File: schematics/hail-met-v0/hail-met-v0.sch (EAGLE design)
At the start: 8 parts, among them U1 ATMEGA328P, X1 S4B-ZR, Y1 16MHZ

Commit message: updated schematic, added datasheets
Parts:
- removed X1: S4B-ZR, con-jst:S4B-ZR
- added C3: 4700uF, rcl:CPOL-USE5-13
- added C4: 10uF, adafruit:C-USC0805K
- added C5: 10uF, rcl:C-USC0805K
- added CHRG/LBO: ORANGE, adafruit:LEDCHIP-LED0805
- added DONE: GREEN, adafruit:LEDCHIP-LED0805
- added IC1: MCP73871, adafruit:MCP73871
- added JP_BATT, JP_SOLAR: (no value), adafruit:JST_2PIN-SMT-RA
- added PWR: RED, adafruit:LEDCHIP-LED0805
- added R10: 150K, rcl:R-US_M0805
- added R11: 100K, rcl:R-US_M0805
- added R12: 2K, adafruit:R-US_FLIPFLOP
- added R3, R4: (no value), SparkFun-Resistors:1KOHM1/10W1%(0603)
- added R5, R6, R7: 1K, SparkFun-Resistors:1KOHM1/10W1%(0603)
- added R8: 1K, rcl:R-US_M0805
- added R9: 10K, adafruit:R-US_FLIPFLOP
- added U$2: 10118193, MicroUSB:10118193
- added U2: TLC5917ID, Texas Instruments_By_element14_Batch_1:TLC5917ID
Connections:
- new net LED_OE: U1.PB1(OC1A), U2.~OE(ED2)
- new net N$10: U2.~OUT5
- new net N$11: U2.~OUT6
- new net N$12: U2.~OUT7
- new net N$13: R10.2, R8.2, R9.2
- new net N$14: U2.LE(ED1)
- new net N$15: U2.SDI
- new net N$16: U2.CLK
- new net N$17: IC1.VPCC, R3.2, R4.1
- new net N$18: IC1.PROG3, R11.2
- new net N$19: IC1./PG, PWR.C
- new net N$20: DONE.C, IC1.STAT2
- new net N$21: CHRG/LBO.C, IC1.STAT1/LBO
- new net N$22: CHRG/LBO.A, R7.1
- new net N$23: DONE.A, R6.1
- new net N$24: PWR.A, R5.1
- new net N$26: C5.1, IC1.VBAT1, IC1.VBAT2, IC1.VBAT3, JP_BATT.1
- new net N$3: IC1.THERM, R8.1
- new net N$5: U2.~OUT0
- new net N$6: U2.~OUT1
- new net N$7: U2.~OUT2
- new net N$8: U2.~OUT3
- new net N$9: U2.~OUT4
- new net PROG1: IC1.PROG1, R12.2
- new net VCC: C3.+, C4.1, IC1./TE, IC1.CE, IC1.IN1, IC1.IN2, IC1.PROG2, IC1.SEL, JP_SOLAR.1, R4.2, R5.2, R6.2, R7.2, U$2.VBUS
- net 3.3V: now also U2.VDD
- net GND: now also C3.-, C4.2, C5.2, IC1.GND1, IC1.GND2, JP_BATT.2, JP_SOLAR.2, R10.1, R11.1, R12.1, R3.1, R9.1, U$2.GND, U2.GND
- net VIN: now also IC1.OUT1, IC1.OUT2
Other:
- note added: "1.0K = 1000mA"
- note added: "10K NTC Thermistor:"
- note added: "2.0K = 500mA"
- note added: "Charge Rate = 1000V/PROG1"
- note added: "JST jack to batteries"
- note added: "LED Driver"
- note added: "NEED TO SET THIS TO VREG. For 6V solar panel, use 1KOhm / 1KOhm"
- note added: "No Thermistor:"
- note added: "Power input (USB, Solar)"
- note added: "RT1 = 0, RT2 = 10K"
- note added: "RT1 = TBD, RT2 = TBD"
- note added: "Voltage regulator for microcontroller"
- note removed: "JST jack from batteries"
- moved on the sheet: C1, C2, R1, R2, U$1

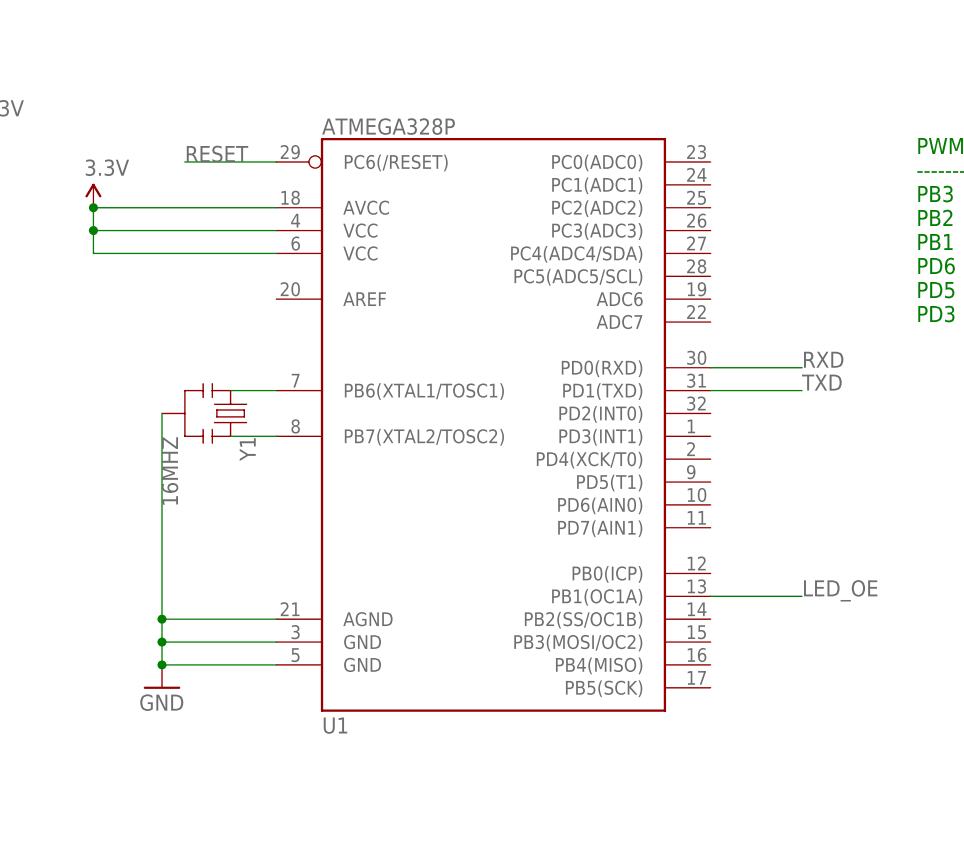
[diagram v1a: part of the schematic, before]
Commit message: cleaned up EAGLE temp files
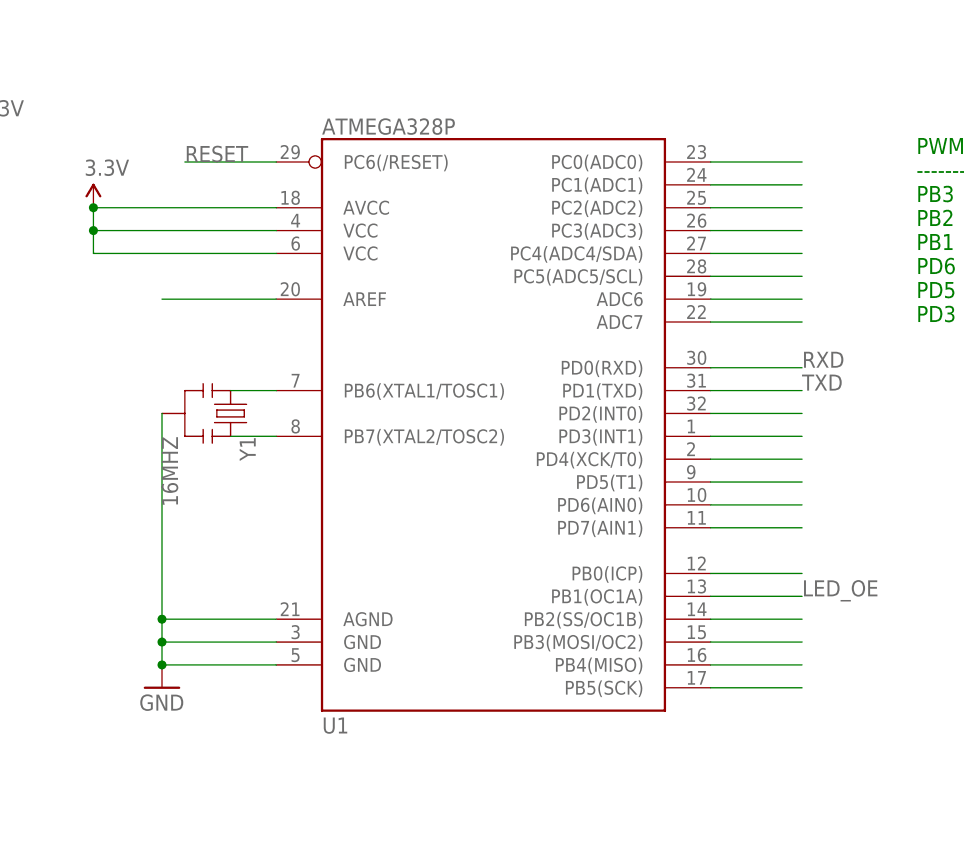
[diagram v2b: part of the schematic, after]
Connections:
- new net N$25: U1.AREF
- new net N$27: U1.PC0(ADC0)
- new net N$28: U1.PC1(ADC1)
- new net N$29: U1.PC2(ADC2)
- new net N$30: U1.PC3(ADC3)
- new net N$31: U1.PC4(ADC4/SDA)
- new net N$32: U1.PC5(ADC5/SCL)
- new net N$33: U1.ADC6
- new net N$34: U1.ADC7
- new net N$35: U1.PD2(INT0)
- new net N$36: U1.PD3(INT1)
- new net N$37: U1.PD4(XCK/T0)
- new net N$38: U1.PD5(T1)
- new net N$39: U1.PD6(AIN0)
- new net N$40: U1.PD7(AIN1)
- new net N$41: U1.PB0(ICP)
- new net N$42: U1.PB2(SS/OC1B)
- new net N$43: U1.PB3(MOSI/OC2)
- new net N$44: U1.PB4(MISO)
- new net N$45: U1.PB5(SCK)
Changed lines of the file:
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@@
+</segment>
+</net>
+<net name="N$25" class="0">
+<segment>
+<pinref part="U1" gate="G$1" pin="AREF"/>
+<wire x1="83.82" y1="71.12" x2="71.12" y2="71.12" width="0.1524" layer="91"/>
+</segment>
+</net>
+<net name="N$27" class="0">
+<segment>
+<pinref part="U1" gate="G$1" pin="PC0(ADC0)"/>
+<wire x1="132.08" y1="86.36" x2="142.24" y2="86.36" width="0.1524" layer="91"/>
+</segment>
+</net>
+<net name="N$28" class="0">
+<segment>
+<pinref part="U1" gate="G$1" pin="PC1(ADC1)"/>
+<wire x1="132.08" y1="83.82" x2="142.24" y2="83.82" width="0.1524" layer="91"/>
+</segment>
+</net>
+<net name="N$29" class="0">
+<segment>
+<pinref part="U1" gate="G$1" pin="PC2(ADC2)"/>
+<wire x1="132.08" y1="81.28" x2="142.24" y2="81.28" width="0.1524" layer="91"/>
+</segment>
+</net>
+<net name="N$30" class="0">
+<segment>
+<pinref part="U1" gate="G$1" pin="PC3(ADC3)"/>
+<wire x1="132.08" y1="78.74" x2="142.24" y2="78.74" width="0.1524" layer="91"/>
+</segment>
+</net>
+<net name="N$31" class="0">
+<segment>
+<pinref part="U1" gate="G$1" pin="PC4(ADC4/SDA)"/>
+<wire x1="132.08" y1="76.2" x2="142.24" y2="76.2" width="0.1524" layer="91"/>
+</segment>
+</net>
+<net name="N$32" class="0">
+<segment>
+<pinref part="U1" gate="G$1" pin="PC5(ADC5/SCL)"/>
+<wire x1="132.08" y1="73.66" x2="142.24" y2="73.66" width="0.1524" layer="91"/>
+</segment>
+</net>
+<net name="N$33" class="0">
+<segment>
+<pinref part="U1" gate="G$1" pin="ADC6"/>
+<wire x1="132.08" y1="71.12" x2="142.24" y2="71.12" width="0.1524" layer="91"/>
+</segment>
+</net>
+<net name="N$34" class="0">
+<segment>
+<pinref part="U1" gate="G$1" pin="ADC7"/>
+<wire x1="132.08" y1="68.58" x2="142.24" y2="68.58" width="0.1524" layer="91"/>
+</segment>
+</net>
+<net name="N$35" class="0">
+<segment>
+<pinref part="U1" gate="G$1" pin="PD2(INT0)"/>
+<wire x1="132.08" y1="58.42" x2="142.24" y2="58.42" width="0.1524" layer="91"/>
+</segment>
+</net>
+<net name="N$36" class="0">
+<segment>
+<pinref part="U1" gate="G$1" pin="PD3(INT1)"/>
+<wire x1="132.08" y1="55.88" x2="142.24" y2="55.88" width="0.1524" layer="91"/>
+</segment>
+</net>
+<net name="N$37" class="0">
+<segment>
+<pinref part="U1" gate="G$1" pin="PD4(XCK/T0)"/>
+<wire x1="132.08" y1="53.34" x2="142.24" y2="53.34" width="0.1524" layer="91"/>
+</segment>
+</net>
+<net name="N$38" class="0">
+<segment>
+<pinref part="U1" gate="G$1" pin="PD5(T1)"/>
+<wire x1="132.08" y1="50.8" x2="142.24" y2="50.8" width="0.1524" layer="91"/>
+</segment>
+</net>
+<net name="N$39" class="0">
+<segment>
+<pinref part="U1" gate="G$1" pin="PD6(AIN0)"/>
+<wire x1="132.08" y1="48.26" x2="142.24" y2="48.26" width="0.1524" layer="91"/>
+</segment>
+</net>
+<net name="N$40" class="0">
+<segment>
+<pinref part="U1" gate="G$1" pin="PD7(AIN1)"/>
+<wire x1="132.08" y1="45.72" x2="142.24" y2="45.72" width="0.1524" layer="91"/>
+</segment>
+</net>
+<net name="N$41" class="0">
+<segment>
+<pinref part="U1" gate="G$1" pin="PB0(ICP)"/>
+<wire x1="132.08" y1="40.64" x2="142.24" y2="40.64" width="0.1524" layer="91"/>
+</segment>
+</net>
+<net name="N$42" class="0">
+<segment>
+<pinref part="U1" gate="G$1" pin="PB2(SS/OC1B)"/>
+<wire x1="132.08" y1="35.56" x2="142.24" y2="35.56" width="0.1524" layer="91"/>
+</segment>
+</net>
+<net name="N$43" class="0">
+<segment>
+<pinref part="U1" gate="G$1" pin="PB3(MOSI/OC2)"/>
+<wire x1="132.08" y1="33.02" x2="142.24" y2="33.02" width="0.1524" layer="91"/>
+</segment>
+</net>
+<net name="N$44" class="0">
+<segment>
+<pinref part="U1" gate="G$1" pin="PB4(MISO)"/>
+<wire x1="132.08" y1="30.48" x2="142.24" y2="30.48" width="0.1524" layer="91"/>
+</segment>
+</net>
+<net name="N$45" class="0">
+<segment>
+<pinref part="U1" gate="G$1" pin="PB5(SCK)"/>
+<wire x1="132.08" y1="27.94" x2="142.24" y2="27.94" width="0.1524" layer="91"/>
 </segment>
 </net>

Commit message: updated schematic
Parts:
- added C6: 0.1uF, SparkFun-Capacitors:0.1UF-25V-5%(0603)
- added FTDI: (no value), SparkFun:M06SIP
- added JP10, JP11, JP9, LED0, LED1, LED2, LED3, LED4, LED5, LED6, LED7: M02PTH, SparkFun-Connectors:M02PTH
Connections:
- net N$26 renamed VBATT
- net N$32 renamed PC5
- net VCC renamed VCHG
- removed net N$15: U2.SDI
- removed net N$16: U2.CLK
- removed net N$43: U1.PB3(MOSI/OC2)
- removed net N$45: U1.PB5(SCK)
- new net CTS: C6.2, FTDI.2
- new net DTR: FTDI.6
- new net LED_CLK: U1.PB5(SCK), U2.CLK
- new net LED_SDI: U1.PB3(MOSI/OC2), U2.SDI
- net 3.3V: now also FTDI.3, LED0.1, LED1.1, LED2.1, LED3.1, LED4.1, LED5.1, LED6.1, LED7.1
- net GND: now also FTDI.1
- net N$10: now also LED5.2
- net N$11: now also LED6.2
- net N$12: now also LED7.2
- net N$5: now also LED0.2
- net N$6: now also LED1.2
- net N$7: now also LED2.2
- net N$8: now also LED3.2
- net N$9: now also LED4.2
- net RESET: now also C6.1
- net RXD: now also FTDI.4
- net TXD: now also FTDI.5
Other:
- note added: "Bluetooth"
- note added: "DONE"
- note added: "Design: Validate:"
- note added: "Done, need VCC resistor check"
- moved on the sheet: C1, C2, R1, R2, U$1, U2

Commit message: worked on schematic
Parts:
- removed JP10, JP9, LED0, LED1, LED2, LED3, LED4, LED5, LED6, LED7: M02PTH, SparkFun-Connectors:M02PTH
- added ATM_PB, ATM_PC, ATM_PD, ATM_PWR, JP3, JP4: (no value), SparkFun-Connectors:M08LOCK
- added C10, C9: (no value), adafruit:C-USC0805K
- added C7: 10uF, SparkFun-Passives:CAP0805
- added C8: 22pF, SparkFun-Passives:CAP0805
- added LED0-IL, LED0-IR, LED0-LF, LED1-LM, LED2-LR, LED3-HR, LED4-RF, LED5-RM, LED6-RR, LED7-HF, MIC, SPK_L, SPK_R: M02PTH, SparkFun-Connectors:M02PTH
- added R13: 1K, SparkFun-Passives:RESISTOR0805-RES
- added R14: 10K, SparkFun-Passives:RESISTOR0805-RES
- added R15: 150K, SparkFun-Passives:RESISTOR0805-RES
- added R16, R17, R18, R19, R20, R21, R22, R23, R24: (no value), SparkFun-Passives:RESISTOR0805-RES
- added R25, R26, R27, R28: 20k, SparkFun-Passives:RESISTOR0805-RES
- added U$3: RN52, RN52:RN52
- added U$4: LM4871, SparkFun:LM4871
- C1: value 10uF -> 0.1uF; device SparkFun-Capacitors:10UF-6.3V-20%(0603) -> SparkFun-Passives:CAP0805
- C2: value 22pF -> 0.1uF; device SparkFun-Capacitors:22PF-50V-5%(0603) -> adafruit:C-USC0805K
- C6: device SparkFun-Capacitors:0.1UF-25V-5%(0603) -> adafruit:C-USC0805K
- FTDI: device SparkFun:M06SIP -> SparkFun-Connectors:M06LOCK
- R1: value 240 -> (none); device SparkFun-Resistors:240OHM1/10W1%(0603) -> SparkFun-Passives:RESISTOR0805-RES
- R10: value 150K -> (none); device rcl:R-US_M0805 -> SparkFun-Passives:RESISTOR0805-RES
- R11: device rcl:R-US_M0805 -> SparkFun-Passives:RESISTOR0805-RES
- R12: value 2K -> 1K; device adafruit:R-US_FLIPFLOP -> SparkFun-Passives:RESISTOR0805-RES
- R2: value 390 -> (none); device SparkFun-Resistors:240OHM1/10W1%(0603) -> SparkFun-Passives:RESISTOR0805-RES
- R3, R4, R5, R6: device SparkFun-Resistors:1KOHM1/10W1%(0603) -> SparkFun-Passives:RESISTOR0805-RES
- R7: value 1K -> 2K; device SparkFun-Resistors:1KOHM1/10W1%(0603) -> SparkFun-Passives:RESISTOR0805-RES
- R8: value 1K -> 240; device rcl:R-US_M0805 -> SparkFun-Passives:RESISTOR0805-RES
- R9: value 10K -> 390; device adafruit:R-US_FLIPFLOP -> SparkFun-Passives:RESISTOR0805-RES
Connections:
- new net MIC_L+: JP3.8, JP4.8
- new net MIC_L-: JP3.6, JP4.6
- new net MIC_R+: JP3.7, JP4.7
- new net MIC_R-: JP3.5, JP4.5
- new net N$15: ATM_PC.1, ATM_PD.1
- new net N$16: ATM_PC.2, ATM_PD.2
- new net N$26: ATM_PC.3, ATM_PD.3, ATM_PWR.3
- new net N$32: ATM_PC.4, ATM_PD.4, ATM_PWR.4
- new net N$43: ATM_PC.5, ATM_PD.5, ATM_PWR.5
- new net N$45: ATM_PC.6, ATM_PD.6, ATM_PWR.6
- new net N$46: ATM_PC.7, ATM_PD.7, ATM_PWR.7
- new net N$47: ATM_PC.8, ATM_PD.8, ATM_PWR.8
- new net N$48: ATM_PB.1
- new net N$49: ATM_PB.2
- new net N$50: ATM_PB.3
- new net N$51: ATM_PB.4
- new net N$52: ATM_PB.5
- new net N$53: ATM_PB.6
- new net N$54: ATM_PB.7
- new net N$55: ATM_PB.8
- new net N$56: R1.1, U2.R-EXT
- new net N$57: LED0-LF.2, R2.1
- new net N$58: LED4-RF.2, R21.1
- new net N$59: LED5-RM.2, R20.1
- new net N$60: LED6-RR.2, R19.1
- new net N$61: LED7-HF.2, R18.1
- new net N$62: LED3-HR.2, R17.1
- new net N$63: LED1-LM.2, R10.1
- new net N$64: LED2-LR.2, R16.1
- new net N$65: LED0-IL.2, R22.1
- new net N$66: LED0-IR.2, R23.1
- new net N$67: JP11.2, R24.1
- new net N$68: R24.2
- new net N$69: U$3.UART_TX
- new net N$70: U$3.UART_RX
- new net N$71: R26.2, R27.2, U$4.IN-
- new net N$72: C9.1, R25.1
- new net N$73: C9.2, U$3.SPKR_L+
- new net N$74: C2.1, U$4.BYPASS
- new net N$75: R25.2, R28.1, U$4.IN+
- new net N$76: C10.2, U$3.SPKR_R+
- new net N$77: C10.1, R26.1
- new net SPKR_L: R28.2, SPK_L.1
- new net SPKR_L+: JP3.1, JP4.1
- new net SPKR_L-: JP3.3, JP4.3
- new net SPKR_R: R27.1, SPK_R.1
- new net SPKR_R+: JP3.2, JP4.2
- new net SPKR_R-: JP3.4, JP4.4
- net 3.3V: now also C6.1, C8.1, JP11.1, LED0-IL.1, LED0-IR.1, LED0-LF.1, LED1-LM.1, LED2-LR.1, LED3-HR.1, LED4-RF.1, LED5-RM.1, LED6-RR.1, LED7-HF.1, R8.2, U$4.VDD; no longer C2.1, LED0.1, LED1.1, LED2.1, LED3.1, LED4.1, LED5.1, LED6.1, LED7.1, R1.2
- net CTS: now also C1.2; no longer C6.2
- net GND: now also C6.2, C7.2, C8.2, R1.2, R14.1, R15.1, R4.1, R7.1, SPK_L.2, SPK_R.2, U$3.GND0, U$3.GND1, U$3.GND2, U$3.GND3, U$3.GND4, U$3.GND5, U$3.GND6, U$3.GND7, U$3.GND8, U$3.GND9, U$3.SPKR_L-, U$3.SPKR_R-, U$4.GND; no longer C1.2, R10.1, R12.1, R2.1, R3.1
- net N$10: now also R20.2; no longer LED5.2
- net N$11: now also R19.2; no longer LED6.2
- net N$12: now also R18.2; no longer LED7.2
- net N$13: now also R12.2, R14.2, R15.2; no longer R10.2, R8.2, R9.2
- net N$17: now also R3.1, R4.2; no longer R3.2, R4.1
- net N$22: now also R13.1; no longer R7.1
- net N$23: now also R5.1; no longer R6.1
- net N$24: now also R6.1; no longer R5.1
- net N$3: now also R12.1; no longer R8.1
- net N$4: now also R8.1, R9.2; no longer R1.1, R2.2
- net N$5: now also R2.2, R22.2; no longer LED0.2
- net N$6: now also R10.2; no longer LED1.2
- net N$7: now also R16.2; no longer LED2.2
- net N$8: now also R17.2; no longer LED3.2
- net N$9: now also R21.2, R23.2; no longer LED4.2
- net PROG1: now also R7.2; no longer R12.2
- net RESET: now also C1.1; no longer C6.1
- net VCHG: now also R13.2, R3.2; no longer R4.2, R7.2
- net VIN: now also ATM_PWR.1, ATM_PWR.2, C7.1; no longer C1.1
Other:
- note added: "Breakout for ATmega328"
- note added: "Names: ------ LED0-LF Left Front LED0-IL Indicator Left LED1-LM Left Middle LED2-LR Left Rear LED3-HR Headlight Front LED4-RF Right Front LED4-IR Indicator Right LED5-RM Right Middle LED6-RR Right Rear LED7-HF Headlight Front"
- note added: "Note: Pin headers used so wires can be soldered directly to board. Design decision based on cost and weight of the helmet."
- note added: "Step-up converter for USB phone port"
- moved on the sheet: C1, C2, C6, JP11, R1, R10, R12, R2, R3, R4, R5, R6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

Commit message: updated schematic, added datasheets
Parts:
- removed C10, C9: (no value), adafruit:C-USC0805K
- removed JP11, LED7-HF: M02PTH, SparkFun-Connectors:M02PTH
- removed R27, R28: 20k, SparkFun-Passives:RESISTOR0805-RES
- added CI_L, CI_R, CO_L, CO_R: (no value), adafruit:C-USC0805K
- added EXT_PWR_JACK, LED7-LB, LED_CREE, NTC_THERM, PWR_BUTTON, SW_BFF, SW_BRR, SW_BSEL, SW_TL, SW_TR: M02PTH, SparkFun-Connectors:M02PTH
- added MPU-6050: (no value), SparkFun-Connectors:M08LOCK
- added RF_L, RF_R, RI_L, RI_R: 20k, SparkFun-Passives:RESISTOR0805-RES
- added RT1: (no value), SparkFun-Passives:RESISTOR0805-RES
- added U$5: TEMT6000, SparkFun:TEMT6000
- R12: value 1K -> (none)
- R15: value 150K -> 1K
- R25, R26: value 20k -> 1K
- RT2: value 10K -> (none)
- renumbered R14 to RT2
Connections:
- removed net N$19: IC1./PG, PWR.C
- removed net N$20: DONE.C, IC1.STAT2
- removed net N$21: CHRG/LBO.C, IC1.STAT1/LBO
- removed net N$35: U1.PD2(INT0)
- removed net N$36: U1.PD3(INT1)
- removed net N$37: U1.PD4(XCK/T0)
- removed net N$68: R24.2
- removed net PC5: U1.PC5(ADC5/SCL)
- new net AMB_IN: R12.1, U$5.E1, U1.PC0(ADC0)
- new net BTH_CMD: U$3.GPIO9, U1.PD3(INT1)
- new net BTH_EVENT: U$3.GPIO2, U1.PD2(INT0)
- new net CHG_DONE: DONE.C, IC1.STAT2, R25.2
- new net CHG_PWR: IC1./PG, PWR.C, R26.2
- new net CHG_STAT1: CHRG/LBO.C, IC1.STAT1/LBO, R15.2
- new net CHG_VOUT: ATM_PWR.1, IC1.OUT1, IC1.OUT2
- new net DEV_EN: U$3.PWREN, U1.PD4(XCK/T0)
- new net EXT_5V: ATM_PWR.3, EXT_PWR_JACK.1
- new net MPU_INT: MPU-6050.3
- new net MPU_SCL: MPU-6050.5, U1.PC5(ADC5/SCL)
- new net MPU_SDA: MPU-6050.6, U1.PC4(ADC4/SDA)
- new net MPU_SYNC: MPU-6050.4
- new net MPU_VIO: MPU-6050.7
- new net N$80: JP_SOLAR.1, PWR_BUTTON.2, U$2.VBUS
- new net SW_BFF: SW_BFF.1
- new net SW_BRR: SW_BRR.1
- new net SW_BSEL: SW_BSEL.1
- new net SW_TL: SW_TL.1
- new net SW_TR: SW_TR.1
- net 3.3V: now also LED7-LB.1, LED_CREE.1, MPU-6050.1, R13.2, R15.1, R25.1, R26.1, R5.2, R6.2, U$5.C1; no longer JP11.1, LED7-HF.1
- net GND: now also EXT_PWR_JACK.2, MPU-6050.2, MPU-6050.8, NTC_THERM.2, R12.2, SW_BFF.2, SW_BRR.2, SW_BSEL.2, SW_TL.2, SW_TR.2; no longer R15.1
- net N$13: now also NTC_THERM.1, RT1.2; no longer R12.2, R15.2
- net N$26: no longer ATM_PWR.3
- net N$27: now also CO_R.2, SPK_R.1; no longer U1.PC0(ADC0)
- net N$3: now also RT1.1; no longer R12.1
- net N$31: now also CO_L.2, SPK_L.1; no longer U1.PC4(ADC4/SDA)
- net N$61: now also LED7-LB.2; no longer LED7-HF.2
- net N$67: now also LED_CREE.2; no longer JP11.2
- net N$71: now also RF_R.2, RI_R.2; no longer R26.2, R27.2
- net N$72: now also CI_L.1, RI_L.1; no longer C9.1, R25.1
- net N$73: now also CI_L.2; no longer C9.2
- net N$75: now also RF_L.1, RI_L.2; no longer R25.2, R28.1
- net N$76: now also CI_R.2; no longer C10.2
- net N$77: now also CI_R.1, RI_R.1; no longer C10.1, R26.1
- net SPKR_L: now also CO_L.1, RF_L.2, U$4.V02; no longer R28.2, SPK_L.1
- net SPKR_R: now also CO_R.1, RF_R.1, U$4.V01; no longer R27.1, SPK_R.1
- net VCHG: now also PWR_BUTTON.1; no longer JP_SOLAR.1, R13.2, R5.2, R6.2, U$2.VBUS
- net VIN: no longer ATM_PWR.1, IC1.OUT1, IC1.OUT2
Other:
- note added: "Accelerometer header"
- note added: "Ambient Light Sensor"
- note added: "Buttons"
- note added: "FTDI header (angle pins)"
- note added: "Names: ------ LED0-LF Left Front LED0-IL Indicator Left LED1-LM Left Middle LED2-LR Left Rear LED3-HR Headlight Front LED4-RF Right Front LED4-IR Indicator Right LED5-RM Right Middle LED6-RR Right Rear LED7-LB Low-battery indicator"
- note added: "Names: ------ SW-TL Turn Left SW-TR Turn Right SW-BFF Bluetooth Fast Forward SW-BRR Bluetooth Rewind SW-BSEL Bluetooth Select"
- note added: "Thermistor: https://www.sparkfun.com/products/250"
- note added: "Voltage Regulator: LM317DCYR 296-12602-1-ND"
- note removed: "Names: ------ LED0-LF Left Front LED0-IL Indicator Left LED1-LM Left Middle LED2-LR Left Rear LED3-HR Headlight Front LED4-RF Right Front LED4-IR Indicator Right LED5-RM Right Middle LED6-RR Right Rear LED7-HF Headlight Front"
- moved on the sheet: ATM_PB, ATM_PC, ATM_PD, ATM_PWR, C2, C3, C4, C5, C6, CHRG/LBO, DONE, FTDI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
